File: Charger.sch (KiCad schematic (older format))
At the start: 65 parts, among them Q1 AO4407A, Q10 AO4468, Q11 AO4468, Q8 AO4468, Q9 AO4468, U1 bq2477x

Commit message: Lots of changes for MFG: parts info
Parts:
- C10, C11, C48, C49, C50, C8: SKU (none) -> CC0805KKX5R8BB106
- C12, C13, C14, C15, C4, C44, C7, C9: SKU (none) -> CL21A226MAQNNNE
- C16, C17: SKU (none) -> RVT1V221M0810
- D1, D9: SKU (none) -> 304040005
- L1: SKU (none) -> MWSA0603-2R2MT
- Q10, Q11, Q8, Q9: SKU (none) -> AO4468
- U1: SKU (none) -> BQ24780S
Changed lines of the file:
@@
 F 2 "SmartBattery:QFN40P400X400X80-29N" H 3850 4400 50  0001 C CNN
 F 3 "" H 3850 4400 50  0001 C CNN
+F 4 "BQ24780S" H 3850 4400 50  0001 C CNN "SKU"
 	1    3850 4400
 	1    0    0    -1
@@
 F 2 "SmartBattery:MWSA0603" H 6250 3100 50  0001 C CNN
 F 3 "~" H 6250 3100 50  0001 C CNN
+F 4 "MWSA0603-2R2MT" V 6250 3100 50  0001 C CNN "SKU"
 	1    6250 3100
 	0    1    1    0
@@
 F 2 "Capacitor_SMD:C_0805_2012Metric" H 8500 3250 50  0001 C CNN
 F 3 "~" H 8500 3250 50  0001 C CNN
+F 4 "CC0805KKX5R8BB106" H 8500 3250 50  0001 C CNN "SKU"
 	1    8500 3250
 	1    0    0    -1
@@
 F 2 "Capacitor_SMD:C_0805_2012Metric" H 8350 3250 50  0001 C CNN
 F 3 "~" H 8350 3250 50  0001 C CNN
+F 4 "CC0805KKX5R8BB106" H 8350 3250 50  0001 C CNN "SKU"
 	1    8350 3250
 	1    0    0    -1
@@
 F 2 "Capacitor_SMD:C_0805_2012Metric" H 8200 3250 50  0001 C CNN
 F 3 "~" H 8200 3250 50  0001 C CNN
+F 4 "CC0805KKX5R8BB106" H 8200 3250 50  0001 C CNN "SKU"
 	1    8200 3250
 	1    0    0    -1
@@
 F 2 "Capacitor_SMD:C_0805_2012Metric" H 7700 2300 50  0001 C CNN
 F 3 "~" H 7700 2300 50  0001 C CNN
+F 4 "CL21A226MAQNNNE" H 7700 2300 50  0001 C CNN "SKU"
 	1    7700 2300
 	1    0    0    -1
@@
 F 2 "Capacitor_SMD:C_0805_2012Metric" H 8000 2300 50  0001 C CNN
 F 3 "~" H 8000 2300 50  0001 C CNN
+F 4 "CL21A226MAQNNNE" H 8000 2300 50  0001 C CNN "SKU"
 	1    8000 2300
 	1    0    0    -1
@@
 F 2 "Capacitor_SMD:C_0805_2012Metric" H 8350 2300 50  0001 C CNN
 F 3 "~" H 8350 2300 50  0001 C CNN
+F 4 "CL21A226MAQNNNE" H 8350 2300 50  0001 C CNN "SKU"
 	1    8350 2300
 	1    0    0    -1
@@
 F 2 "Capacitor_SMD:C_0805_2012Metric" H 8650 2300 50  0001 C CNN
 F 3 "~" H 8650 2300 50  0001 C CNN
+F 4 "CL21A226MAQNNNE" H 8650 2300 50  0001 C CNN "SKU"
 	1    8650 2300
 	1    0    0    -1
@@
 F 2 "Capacitor_SMD:C_0805_2012Metric" H 8900 2300 50  0001 C CNN
 F 3 "~" H 8900 2300 50  0001 C CNN
+F 4 "CL21A226MAQNNNE" H 8900 2300 50  0001 C CNN "SKU"
 	1    8900 2300
 	1    0    0    -1
@@
 F 2 "Capacitor_SMD:C_0805_2012Metric" H 9200 2300 50  0001 C CNN
 F 3 "~" H 9200 2300 50  0001 C CNN
+F 4 "CL21A226MAQNNNE" H 9200 2300 50  0001 C CNN "SKU"
 	1    9200 2300
 	1    0    0    -1
@@
 F 2 "Capacitor_SMD:C_0805_2012Metric" H 9500 2300 50  0001 C CNN
 F 3 "~" H 9500 2300 50  0001 C CNN
+F 4 "CL21A226MAQNNNE" H 9500 2300 50  0001 C CNN "SKU"
 	1    9500 2300
 	1    0    0    -1
@@
 F 2 "Capacitor_SMD:C_Elec_8x10.2" H 9800 2300 50  0001 C CNN
 F 3 "~" H 9800 2300 50  0001 C CNN
+F 4 "RVT1V221M0810" H 9800 2300 50  0001 C CNN "SKU"
 	1    9800 2300
 	1    0    0    -1
@@
 F 2 "Capacitor_SMD:C_Elec_8x10.2" H 10100 2300 50  0001 C CNN
 F 3 "~" H 10100 2300 50  0001 C CNN
+F 4 "RVT1V221M0810" H 10100 2300 50  0001 C CNN "SKU"
 	1    10100 2300
 	1    0    0    -1
@@
 F 2 "Capacitor_SMD:C_0805_2012Metric" H 1150 1700 50  0001 C CNN
 F 3 "~" H 1150 1700 50  0001 C CNN
+F 4 "CL21A226MAQNNNE" H 1150 1700 50  0001 C CNN "SKU"
 	1    1150 1700
 	1    0    0    -1
@@
 F 2 "Diode_SMD:D_1206_3216Metric" V 1300 1250 50  0001 C CNN
 F 3 "~" V 1300 1250 50  0001 C CNN
+F 4 "304040005" H 1300 1250 50  0001 C CNN "SKU"
 	1    1300 1250
 	-1   0    0    1
@@
 F 2 "Diode_SMD:D_1206_3216Metric" V 9300 3350 50  0001 C CNN
 F 3 "~" V 9300 3350 50  0001 C CNN
+F 4 "304040005" H 9300 3350 50  0001 C CNN "SKU"
 	1    9300 3350
 	1    0    0    -1
@@
 F 2 "Capacitor_SMD:C_0402_1005Metric" H 4000 1600 50  0001 C CNN
 F 3 "~" H 4000 1600 50  0001 C CNN
+F 4 "CC0805KKX5R8BB106" H 4000 1600 50  0001 C CNN "SKU"
 	1    4000 1600
 	-1   0    0    1
@@
 F 2 "Capacitor_SMD:C_0805_2012Metric" H 4150 1600 50  0001 C CNN
 F 3 "~" H 4150 1600 50  0001 C CNN
+F 4 "CC0805KKX5R8BB106" H 4150 1600 50  0001 C CNN "SKU"
 	1    4150 1600
 	1    0    0    -1
@@
 F 2 "Capacitor_SMD:C_0805_2012Metric" H 4400 1600 50  0001 C CNN
 F 3 "~" H 4400 1600 50  0001 C CNN
+F 4 "CC0805KKX5R8BB106" H 4400 1600 50  0001 C CNN "SKU"
 	1    4400 1600
 	1    0    0    -1
@@
 F 2 "SmartBattery:SOIC-8_Alpha_Omega" H 2300 1700 50  0001 C CNN
 F 3 "~" H 2100 1600 50  0001 C CNN
+F 4 "AO4468" V 2100 1600 50  0001 C CNN "SKU"
 	1    2100 1600
 	0    -1   -1   0
@@
 F 2 "SmartBattery:SOIC-8_Alpha_Omega" H 2900 1700 50  0001 C CNN
 F 3 "~" H 2700 1600 50  0001 C CNN
+F 4 "AO4468" V 2700 1600 50  0001 C CNN "SKU"
 	1    2700 1600
 	0    1    -1   0
@@
 F 2 "SmartBattery:SOIC-8_Alpha_Omega" H 5650 2250 50  0001 C CNN
 F 3 "~" H 5450 2150 50  0001 C CNN
+F 4 "AO4468" H 5450 2150 50  0001 C CNN "SKU"
 	1    5450 2150
 	1    0    0    -1
@@
 F 2 "SmartBattery:SOIC-8_Alpha_Omega" H 5650 3500 50  0001 C CNN
 F 3 "~" H 5450 3400 50  0001 C CNN
+F 4 "AO4468" H 5450 3400 50  0001 C CNN "SKU"
 	1    5450 3400
 	1    0    0    -1

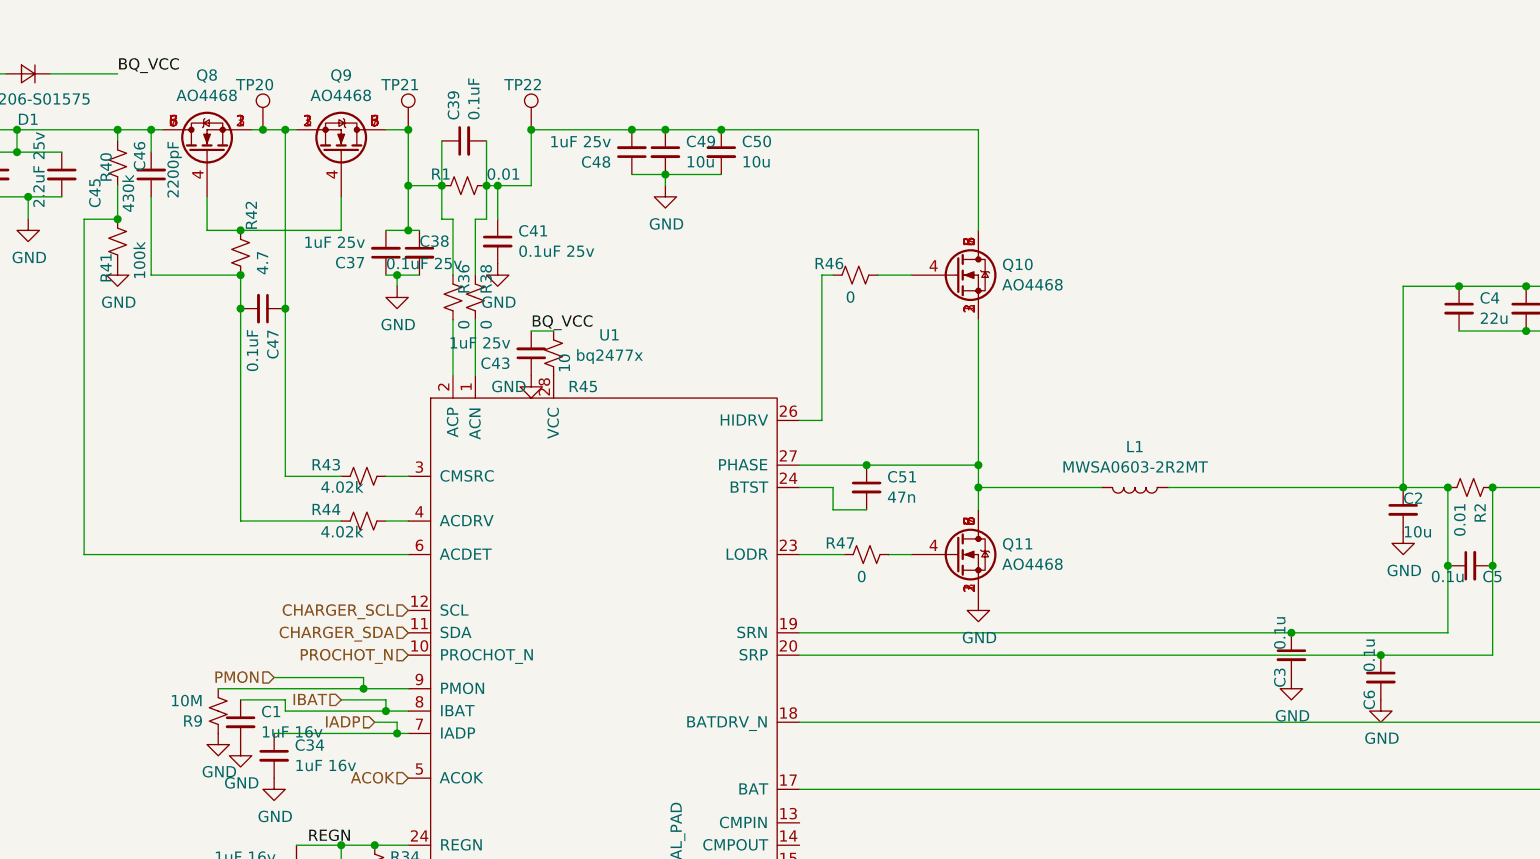
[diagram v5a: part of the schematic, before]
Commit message: Switching over to jlpcb
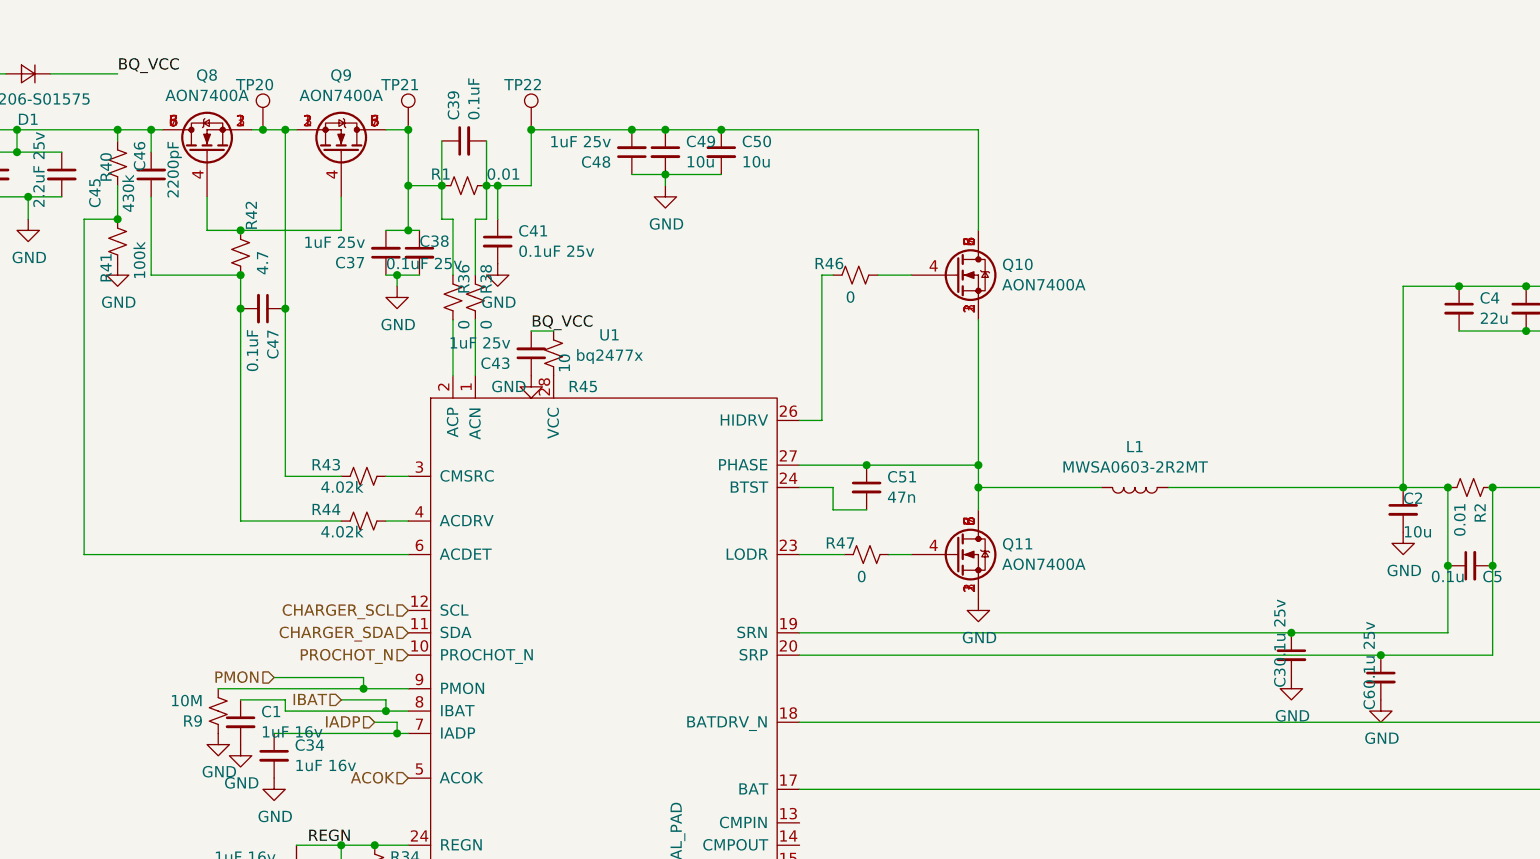
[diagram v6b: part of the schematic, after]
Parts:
- C1: footprint Capacitor_SMD:C_0201_0603Metric -> lc_lib:0402_C; LCSC (none) -> C52923
- C10, C11, C12, C13, C14, C15, C4, C44, C49, C50, C7, C8, C9: footprint Capacitor_SMD:C_0805_2012Metric -> lc_lib:0805_C
- C2: footprint Capacitor_SMD:C_0805_2012Metric -> lc_lib:0805_C; LCSC (none) -> C15850
- C3, C6: value 0.1u -> 0.1u 25v; footprint Capacitor_SMD:C_0603_1608Metric -> lc_lib:0402_C
- C34, C35, C38, C39, C41, C42, C46, C47, C51, C52: footprint Capacitor_SMD:C_0201_0603Metric -> lc_lib:0402_C
- C37, C43, C48: footprint Capacitor_SMD:C_0402_1005Metric -> lc_lib:0402_C
- C45: footprint Capacitor_SMD:C_0603_1608Metric -> lc_lib:0805_C
- C5: footprint Capacitor_SMD:C_0603_1608Metric -> lc_lib:0402_C
- D1, D9: footprint Diode_SMD:D_1206_3216Metric -> lc_lib:SOD-123
- Q10, Q11, Q8, Q9: value AO4468 -> AON7400A; footprint SmartBattery:SOIC-8_Alpha_Omega -> lc_lib:QFN-8_3X3X065P; SKU AO4468 -> AON7400A
- R1, R2: footprint Resistor_SMD:R_1206_3216Metric -> lc_lib:2512_R
- R34, R35, R36, R38, R39, R42, R43, R44, R46, R47, R48: footprint Resistor_SMD:R_0201_0603Metric -> lc_lib:0402_R
- R40, R41, R45: footprint Resistor_SMD:R_1206_3216Metric -> lc_lib:0402_R
- R9: footprint Resistor_SMD:R_0402_1005Metric -> lc_lib:0402_R
